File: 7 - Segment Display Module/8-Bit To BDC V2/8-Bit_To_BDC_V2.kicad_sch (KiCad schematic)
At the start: 42 parts, among them J1 Conn_01x08_Pin, J2 Conn_01x02_Pin, U1 AT28C64B-15PU, U2 AT28C64B-15PU, U3 4056, U4 4056, U5 4056

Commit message: PCB Layout modification
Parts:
- added D10, D11, D4, D5, D6, D7, D8, D9: US1M, Diode_SMD:D_SOD-323_HandSoldering, symbol Diode:US1M
- renumbered R9 to R11, R23 to R22, R24 to R23, R25 to R24, R26 to R25, R27 to R26, R28 to R27, R29 to R28, R30 to R29, R11 to R9
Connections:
- net 1: now also D4.1 (K); no longer J1.1 (Pin_1)
- net 2: now also D5.1 (K); no longer J1.2 (Pin_2)
- net 3: now also D6.1 (K); no longer J1.3 (Pin_3)
- net 4: now also D7.1 (K); no longer J1.4 (Pin_4)
- net 5: now also D8.1 (K); no longer J1.5 (Pin_5)
- net 6: now also D9.1 (K); no longer J1.6 (Pin_6)
- net 7: now also D10.1 (K); no longer J1.7 (Pin_7)
- net 8: now also D11.1 (K); no longer J1.8 (Pin_8)
- new net: D9.2 (A), J1.6 (Pin_6)
- new net: D7.2 (A), J1.4 (Pin_4)
- new net: D11.2 (A), J1.8 (Pin_8)
- new net: D6.2 (A), J1.3 (Pin_3)
- new net: D4.2 (A), J1.1 (Pin_1)
- new net: D5.2 (A), J1.2 (Pin_2)
- new net: D8.2 (A), J1.5 (Pin_5)
- new net: D10.2 (A), J1.7 (Pin_7)
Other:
- moved on the sheet: J1

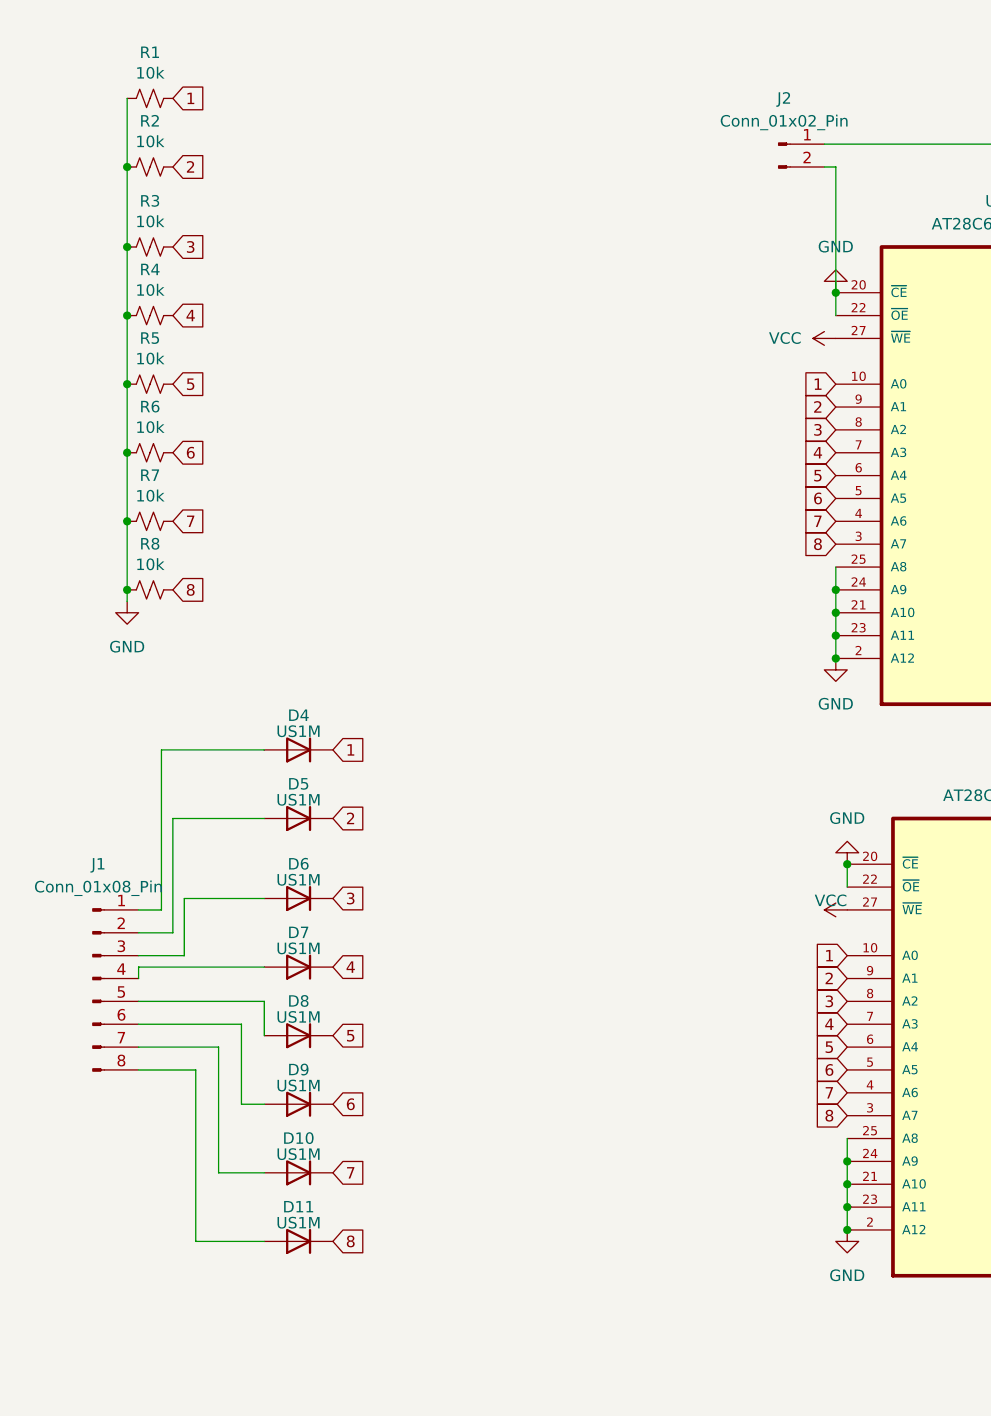
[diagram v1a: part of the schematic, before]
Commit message: Final changes to BCD V2 and switch board
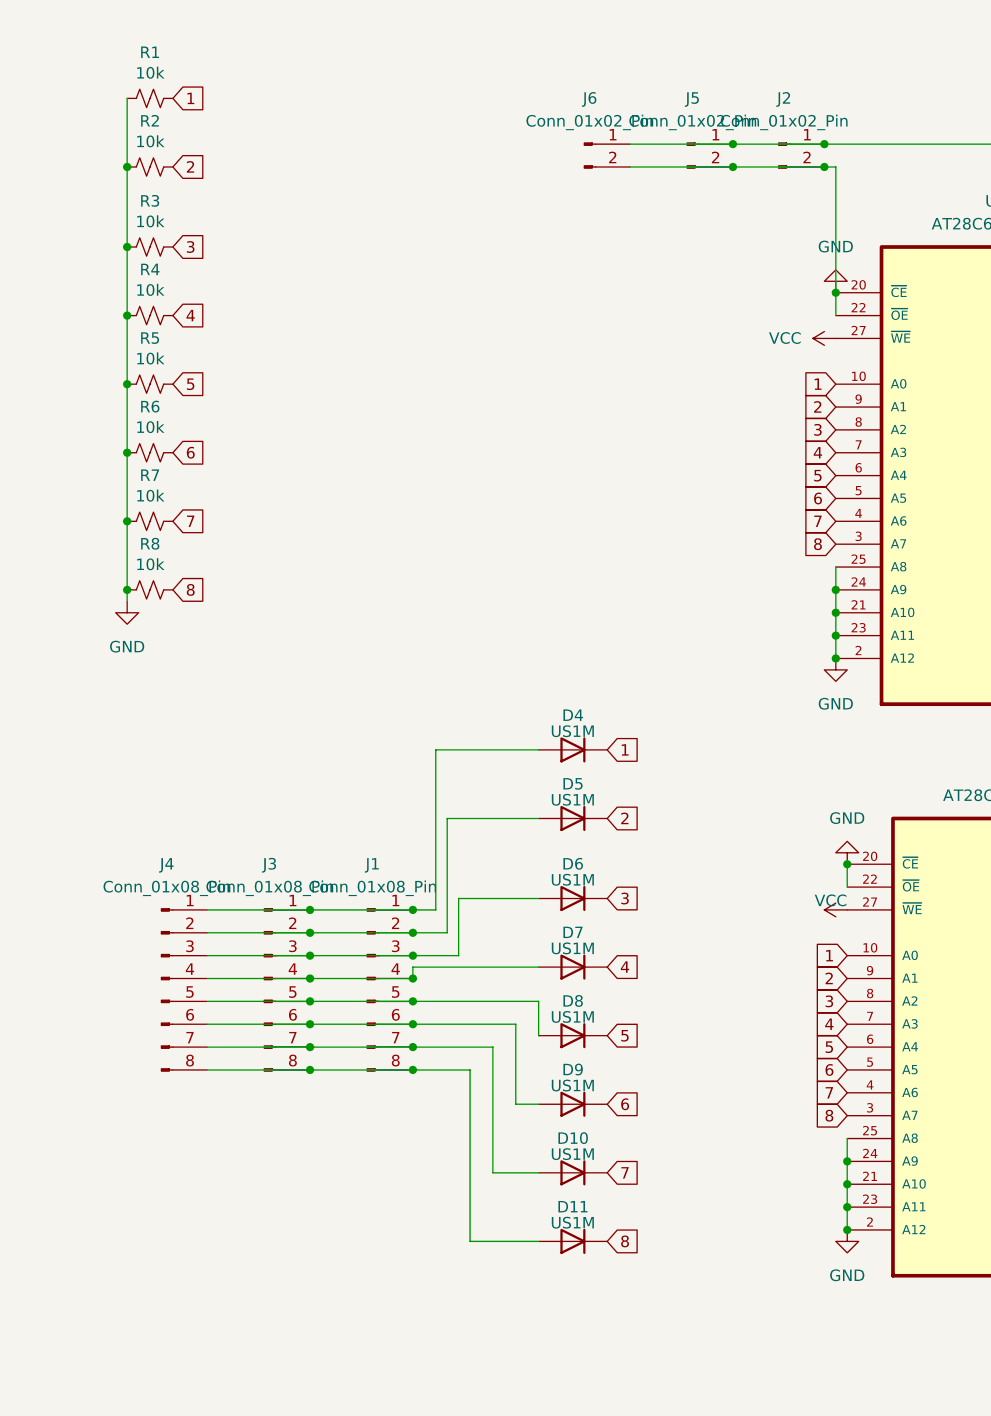
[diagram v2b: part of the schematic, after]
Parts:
- added J3, J4: Conn_01x08_Pin, Connector_PinHeader_2.54mm:PinHeader_2x04_P2.54mm_Vertical, symbol Connector:Conn_01x08_Pin
- added J5, J6: Conn_01x02_Pin, Connector_PinHeader_2.54mm:PinHeader_1x02_P2.54mm_Vertical, symbol Connector:Conn_01x02_Pin
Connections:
- net GND: now also J5.2 (Pin_2), J6.2 (Pin_2)
- net VCC: now also J5.1 (Pin_1), J6.1 (Pin_1)
- net at D9.2 (A), J1.6 (Pin_6): now also J3.6 (Pin_6), J4.6 (Pin_6)
- net at D7.2 (A), J1.4 (Pin_4): now also J3.4 (Pin_4), J4.4 (Pin_4)
- net at D11.2 (A), J1.8 (Pin_8): now also J3.8 (Pin_8), J4.8 (Pin_8)
- net at D6.2 (A), J1.3 (Pin_3): now also J3.3 (Pin_3), J4.3 (Pin_3)
- net at D4.2 (A), J1.1 (Pin_1): now also J3.1 (Pin_1), J4.1 (Pin_1)
- net at D5.2 (A), J1.2 (Pin_2): now also J3.2 (Pin_2), J4.2 (Pin_2)
- net at D8.2 (A), J1.5 (Pin_5): now also J3.5 (Pin_5), J4.5 (Pin_5)
- net at D10.2 (A), J1.7 (Pin_7): now also J3.7 (Pin_7), J4.7 (Pin_7)
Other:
- moved on the sheet: D10, D11, D4, D5, D6, D7, D8, D9, J1
